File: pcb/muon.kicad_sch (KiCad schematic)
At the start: 47 parts, among them J1 Debug Pins, J2 USB_C_Receptacle_USB2.0, SW1 SW_Push, SW2 SW_Push, SW3 Reset, U1 SRV05-4, U2 AP2112, U3 RP2040, U4 W25Q80DVSSIG, Y1 Crystal_GND24_Small

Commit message: v0-2 'release' but not that release-ish
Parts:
- C1, C5: value 5p -> 5pF
- C10, C11, C13, C14, C15, C16, C17, C18, C19, C21: value 100n -> 100nF
- C12, C20: value 1u -> 1uF
- R6, R7: value 27R -> 27

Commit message: minor fixes and shuffle
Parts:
- D3: value PWR LED -> STATUS LED
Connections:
- net +3V3: no longer R9.2
- net SW1: now also U3.40 (GPIO28/ADC2); no longer U3.2 (GPIO0)
- net SW2: now also U3.39 (GPIO27/ADC1); no longer U3.3 (GPIO1)
- net UNDERGLOW: now also U3.34 (GPIO22); no longer U3.40 (GPIO28/ADC2)
- net STATUS: now reaches U3.14 (GPIO11)
- net STATUS: now also R9.2
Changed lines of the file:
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@@
   (no_connect (at 15.24 88.9))
   (no_connect (at 125.73 187.96))
+  (bus_entry (at 93.98 140.97) (size 2.54 2.54)
+    (stroke (width 0) (type default) (color 0 0 0 0))
+  )
   (wire (pts (xy 222.25 55.88) (xy 222.25 57.15))
     (stroke (width 0) (type default) (color 0 0 0 0))
@@
     (stroke (width 0) (type default) (color 0 0 0 0))
   )
+  (wire (pts (xy 127 105.41) (xy 139.7 105.41))
+    (stroke (width 0) (type default) (color 0 0 0 0))
+  )
   (wire (pts (xy 242.57 101.6) (xy 242.57 102.87))
     (stroke (width 0) (type default) (color 0 0 0 0))
@@
     (stroke (width 0) (type default) (color 0 0 0 0))
   )
+  (wire (pts (xy 127 118.11) (xy 139.7 118.11))
+    (stroke (width 0) (type default) (color 0 0 0 0))
+  )
   (wire (pts (xy 212.09 82.55) (xy 218.44 82.55))
     (stroke (width 0) (type default) (color 0 0 0 0))
@@
     (stroke (width 0) (type default) (color 0 0 0 0))
   )
-  (wire (pts (xy 81.28 87.63) (xy 86.36 87.63))
-    (stroke (width 0) (type default) (color 0 0 0 0))
-  )
   (wire (pts (xy 30.48 120.65) (xy 24.13 120.65))
     (stroke (width 0) (type default) (color 0 0 0 0))
   )
-  (wire (pts (xy 81.28 90.17) (xy 86.36 90.17))
-    (stroke (width 0) (type default) (color 0 0 0 0))
-  )
   (wire (pts (xy 86.36 175.26) (xy 86.36 179.07))
     (stroke (width 0) (type default) (color 0 0 0 0))
@@
     (stroke (width 0) (type default) (color 0 0 0 0))
   )
+  (wire (pts (xy 78.74 115.57) (xy 86.36 115.57))
+    (stroke (width 0) (type default) (color 0 0 0 0))
+  )
   (wire (pts (xy 80.01 62.23) (xy 86.36 62.23))
     (stroke (width 0) (type default) (color 0 0 0 0))
   )
-  (wire (pts (xy 20.32 160.02) (xy 21.59 160.02))
+  (wire (pts (xy 13.97 160.02) (xy 21.59 160.02))
     (stroke (width 0) (type default) (color 0 0 0 0))
   )
@@
     (effects (font (size 1.27 1.27)) (justify right bottom))
   )
+  (label "STATUS" (at 78.74 115.57 0)
+    (effects (font (size 1.27 1.27)) (justify left bottom))
+  )
   (label "D+" (at 135.89 82.55 180)
     (effects (font (size 1.27 1.27)) (justify right bottom))
@@
     (effects (font (size 1.27 1.27)) (justify left bottom))
   )
+  (label "STATUS" (at 13.97 160.02 0)
+    (effects (font (size 1.27 1.27)) (justify left bottom))
+  )
   (label "QSPI_CLK" (at 137.16 62.23 180)
     (effects (font (size 1.27 1.27)) (justify right bottom))
@@
     (effects (font (size 1.27 1.27)) (justify right bottom))
   )
-  (label "UNDERGLOW" (at 139.7 120.65 180)
+  (label "UNDERGLOW" (at 139.7 105.41 180)
     (effects (font (size 1.27 1.27)) (justify right bottom))
   )
@@
     (effects (font (size 1.27 1.27)) (justify right bottom))
   )
-  (label "SW1" (at 81.28 87.63 0)
-    (effects (font (size 1.27 1.27)) (justify left bottom))
+  (label "SW1" (at 139.7 120.65 180)
+    (effects (font (size 1.27 1.27)) (justify right bottom))
   )
   (label "QSPI_CS" (at 135.89 74.93 180)
@@
     (effects (font (size 1.27 1.27)) (justify right bottom))
   )
-  (label "SW2" (at 81.28 90.17 0)
-    (effects (font (size 1.27 1.27)) (justify left bottom))
+  (label "SW2" (at 139.7 118.11 180)
+    (effects (font (size 1.27 1.27)) (justify right bottom))
   )
   (symbol (lib_id "power:GND") (at 24.13 115.57 90) (mirror x) (unit 1)
@@
     (in_bom yes) (on_board yes)
     (property "Reference" "D3" (id 0) (at 33.02 163.83 0))
-    (property "Value" "PWR LED" (id 1) (at 33.02 154.94 0))
+    (property "Value" "STATUS LED" (id 1) (at 33.02 154.94 0))
     (property "Footprint" "LED_SMD:LED_0402_1005Metric" (id 2) (at 33.02 160.02 0)
       (effects (font (size 1.27 1.27)) hide)
@@
     (pin "1")
   )
-  (symbol (lib_id "power:+3V3") (at 20.32 160.02 0) (mirror x) (unit 1)
-    (in_bom yes) (on_board yes)
-    (property "Reference" "#PWR0138" (id 0) (at 20.32 156.21 0)
-      (effects (font (size 1.27 1.27)) hide)
-    )
-    (property "Value" "+3V3" (id 1) (at 20.32 168.91 90)
-      (effects (font (size 1.27 1.27)) (justify right))
-    )
-    (property "Footprint" "" (id 2) (at 20.32 160.02 0)
-      (effects (font (size 1.27 1.27)) hide)
-    )
-    (property "Datasheet" "" (id 3) (at 20.32 160.02 0)
-      (effects (font (size 1.27 1.27)) hide)
-    )
-    (pin "1")
-  )
   (symbol (lib_id "power:+3V3") (at 86.36 57.15 90) (unit 1)
     (in_bom yes) (on_board yes)
@@
       (reference "#PWR0137") (unit 1) (value "GND") (footprint "")
     )
-    (path "/a5be9306-c1f9-45a9-ba86-0b3dece932b7"
-      (reference "#PWR0138") (unit 1) (value "+3V3") (footprint "")
-    )
     (path "/df3442eb-11e6-4260-88cb-c180f92e2ce6"
       (reference "C1") (unit 1) (value "5pF") (footprint "Capacitor_SMD:C_0402_1005Metric")
@@
     )
     (path "/02906b2f-52dc-48c9-a9a7-ad38cc44e513"
-      (reference "D3") (unit 1) (value "PWR LED") (footprint "LED_SMD:LED_0402_1005Metric")
+      (reference "D3") (unit 1) (value "STATUS LED") (footprint "LED_SMD:LED_0402_1005Metric")
     )
     (path "/1901dde2-2821-4771-bb70-7c0ba7777492"

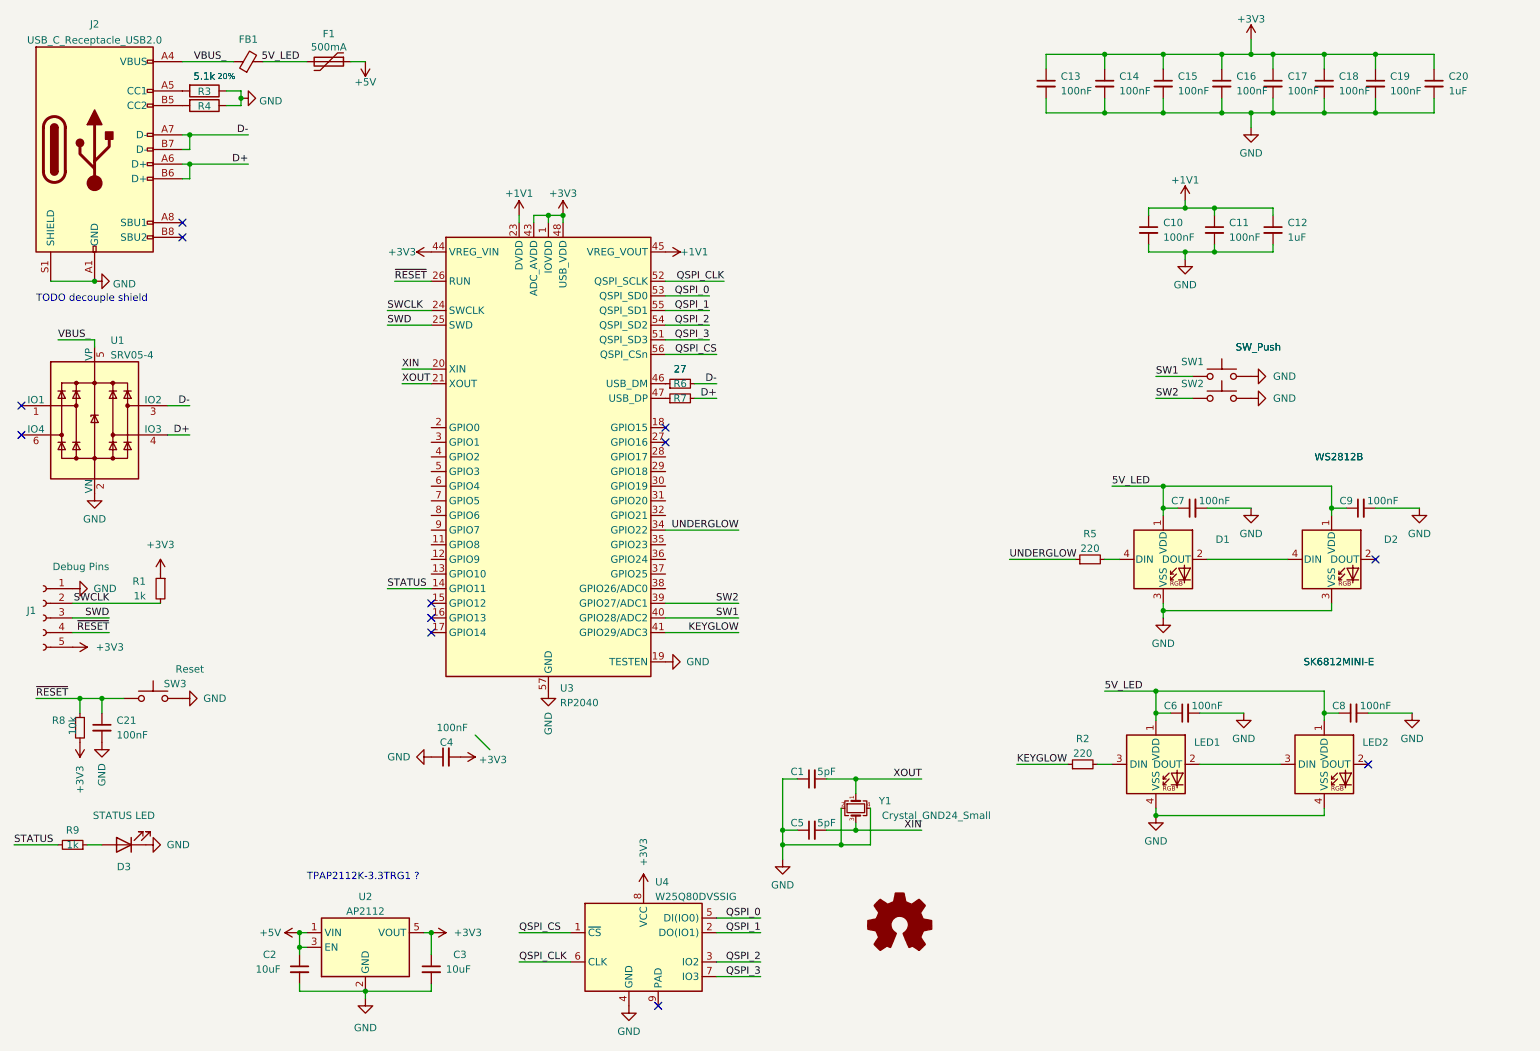
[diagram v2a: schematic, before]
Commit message: all but 3 traces connected
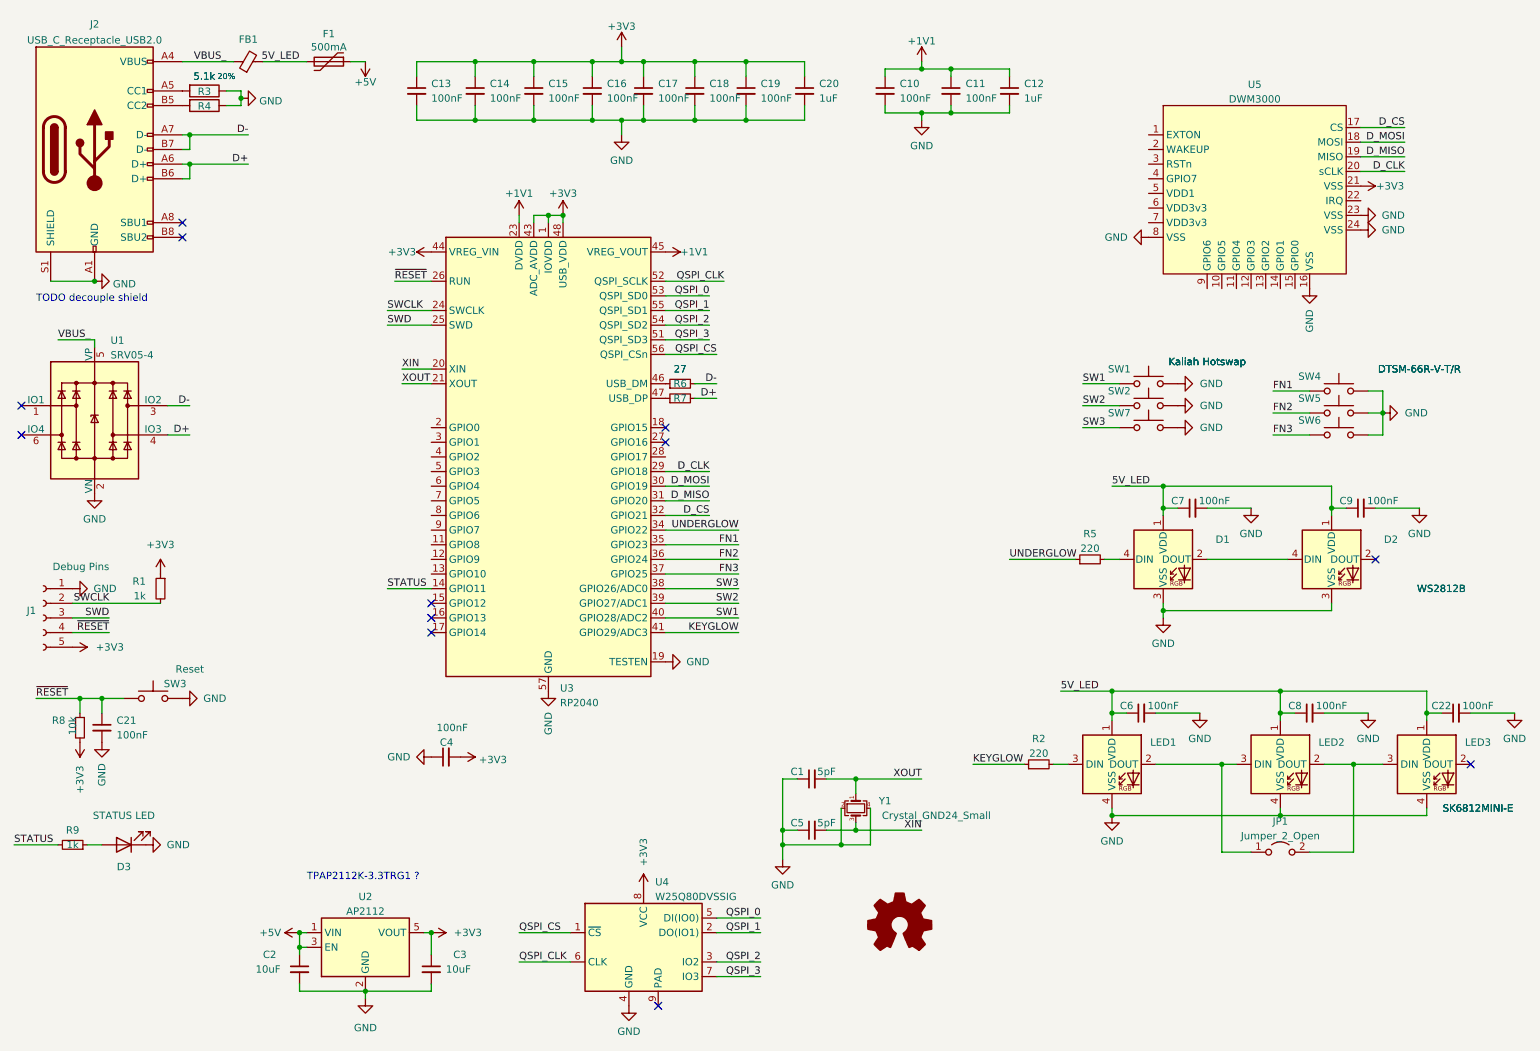
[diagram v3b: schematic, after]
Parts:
- added C22: 100nF, Capacitor_SMD:C_0402_1005Metric, symbol Device:C_Small
- added JP1: Jumper_2_Open, Jumper:SolderJumper-2_P1.3mm_Open_TrianglePad1.0x1.5mm, symbol Jumper:Jumper_2_Open
- added LED3: SK6812MINI-E, marbastlib-various:LED_6028R, symbol marbastlib-various:SK6812MINI-E
- added SW4, SW5, SW6: DTSM-66R-V-T/R, Button_Switch_SMD:SW_Push_1P1T_NO_6x6mm_H9.5mm, symbol Switch:SW_Push
- added SW7: Kaliah Hotswap, Keyswitch:SW_Hotswap_Kailh_MX_1.00u, symbol Switch:SW_Push
- added U5: DWM3000, qorvo:DWM3000, symbol Qorvo:DWM3000
- SW1, SW2: value SW_Push -> Kaliah Hotswap; footprint Keyswitch:SW_Hotswap_Kailh_MX_1.25u -> Keyswitch:SW_Hotswap_Kailh_MX_1.00u
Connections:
- net +3V3: now also U5.21 (VSS)
- net 5V_LED: now also C22.1, LED3.1 (VDD)
- net GND: now also C22.2, LED3.4 (VSS), SW4.2, SW5.2, SW6.2, SW7.2, U5.16 (VSS), U5.23 (VSS), U5.24 (VSS), U5.8 (VSS)
- net at LED1.2 (DOUT), LED2.3 (DIN): now also JP1.1 (A)
- net at LED2.2 (DOUT): now also JP1.2 (B), LED3.3 (DIN)
- net D_CLK: now reaches U3.29 (GPIO18)
- net D_CLK: now also U5.20 (sCLK)
- net D_MOSI: now reaches U3.30 (GPIO19)
- net D_MOSI: now also U5.18 (MOSI)
- net D_MISO: now reaches U3.31 (GPIO20)
- net D_MISO: now also U5.19 (MISO)
- net D_CS: now reaches U3.32 (GPIO21)
- net D_CS: now also U5.17 (CS)
- net FN1: now reaches U3.35 (GPIO23)
- net FN1: now also SW4.1
- net FN2: now reaches U3.36 (GPIO24)
- net FN2: now also SW5.1
- net FN3: now reaches U3.37 (GPIO25)
- net FN3: now also SW6.1
- net SW3: now reaches U3.38 (GPIO26/ADC0)
- net SW3: now also SW7.1
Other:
- moved on the sheet: C10, C11, C12, C13, C14, C15, C16, C17, C18, C19, C20, C6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
